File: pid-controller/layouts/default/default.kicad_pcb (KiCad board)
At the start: 2 copper layers, 210 x 60 mm, 26 parts, among them U17 1kΩ ±1% 100mW, U5 150Ω ±1% 100mW, U7 120Ω ±1% 100mW, U9 100Ω ±1% 100mW

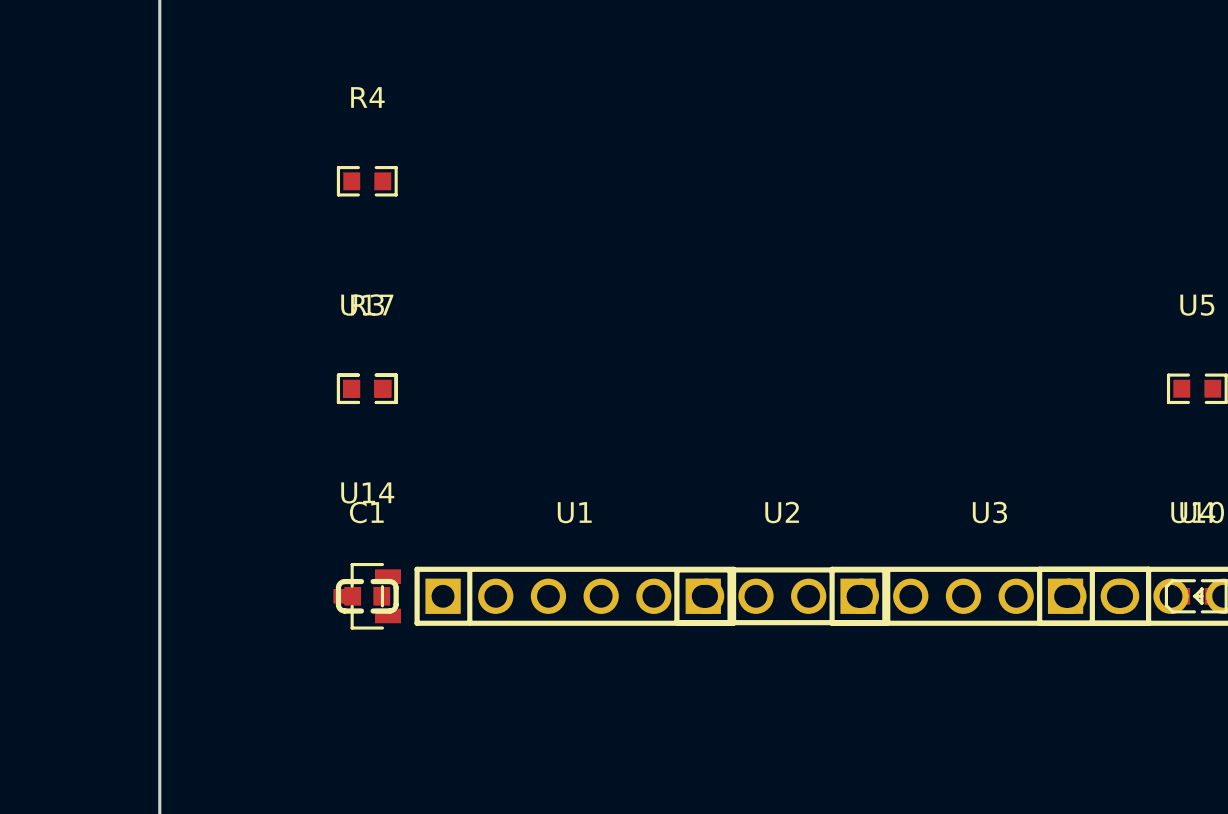
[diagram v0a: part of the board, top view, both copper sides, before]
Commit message: Add AC-DC converter and USB programming header
- Add HLK-PM01 AC-DC converter (100-240V AC → 5V DC @ 600mA)
- Add USB 4-pin header with Schottky diode for programming
- Add AC input connector for mains power
- Update main.ato to use on-board AC power instead of 5V input
- USB power OR-ing allows programming without AC connected

Co-Authored-By: Claude Opus 4.5 <noreply@anthropic.com>
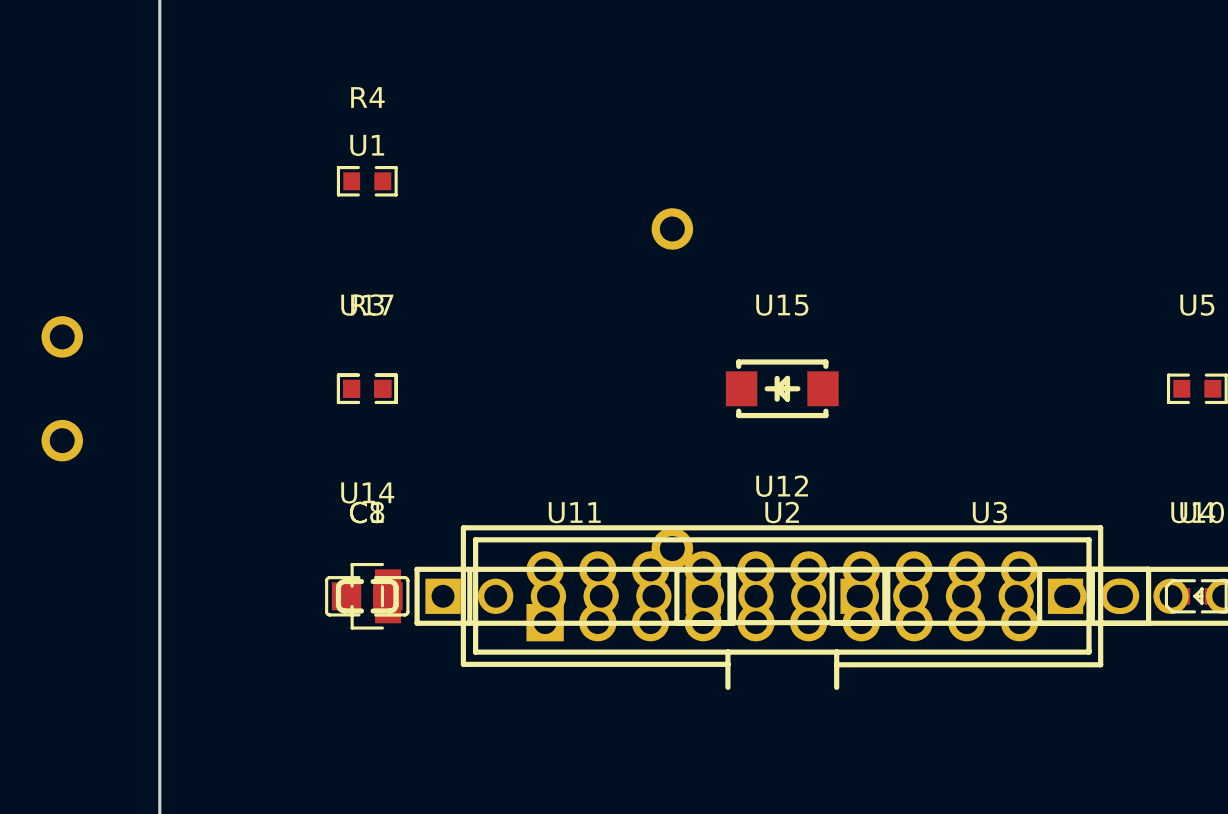
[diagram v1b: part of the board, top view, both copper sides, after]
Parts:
- added C8: 100µF ±20% 6.3V X5R, Murata_Electronics_GRM21BR60J107ME15L:C0805, F.Cu at (0.00, 0.00)
- added U11: , XFCN_PZ254V_11_06P:HDR-TH_6P-P2.54-V-M, F.Cu at (10.0, 0.00)
- added U12: , XFCN_BH254V_20P:CONN-TH_20P-P2.54_BH254V-20P, F.Cu at (20.0, 0.00)
- added U15: , MDD_Microdiode_Electronics_SS14:SMA_L4.2-W2.6-LS5.0-RD_1, F.Cu at (20.0, -10.0)
- U1: footprint XFCN_PZ254V_11_06P:HDR-TH_6P-P2.54-V-M -> HI_LINK_HLK_PM01:PWRM-TH_HLK-PM01
- moved U1 14.1 mm to (0.00, -10.0)
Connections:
- U1 pad 1: power_5v-VCC -> ac_line
- U1 pad 2: GND -> ac_neutral
- U1 pad 3: conn-net-0 -> GND
- U1 pad 4: conn-net-1 -> power_5v-VCC

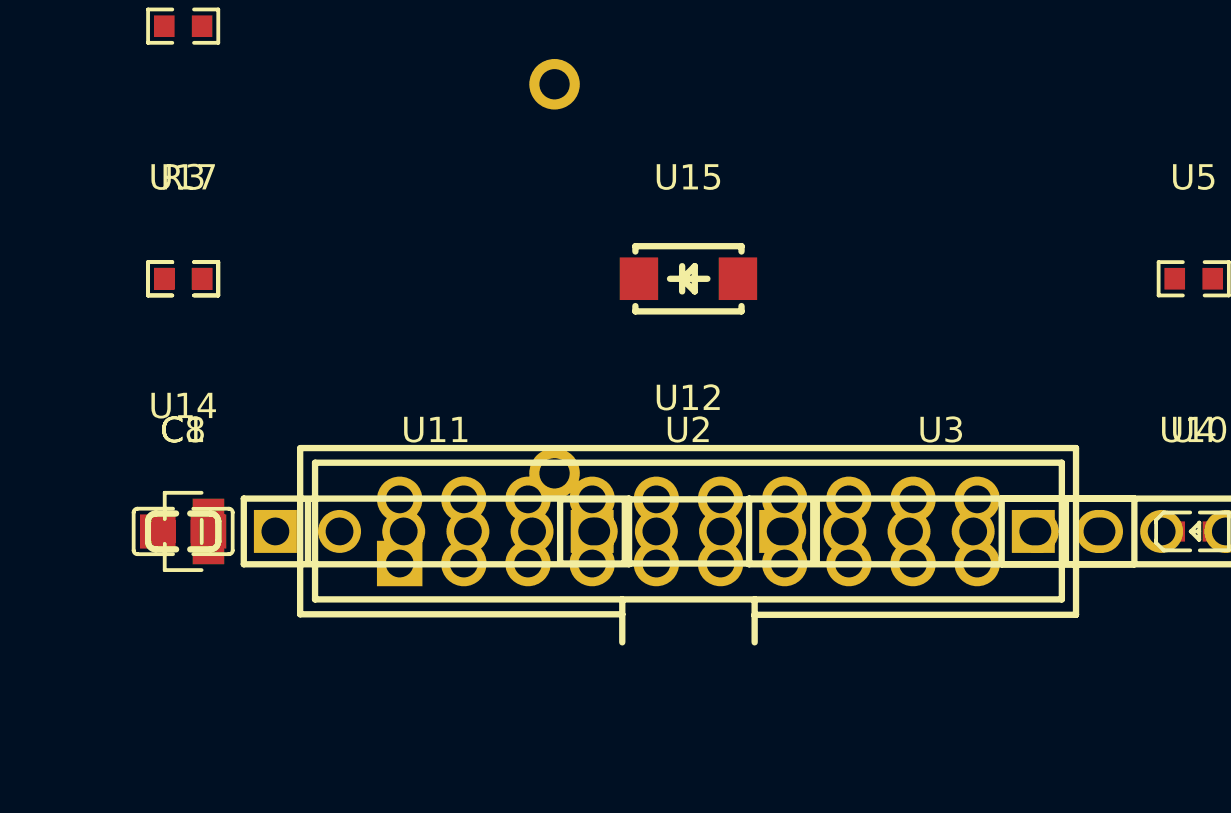
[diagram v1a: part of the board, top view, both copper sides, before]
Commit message: Switch to USB Type-C connector for programming
- Replace 4-pin USB header with USB Type-C (LCSC C393939)
- Add CC resistors (5.1k) for UFP device mode detection
- Pin mapping matches LCSC footprint exactly
- Schottky diode allows USB power when AC is off

Co-Authored-By: Claude Opus 4.5 <noreply@anthropic.com>
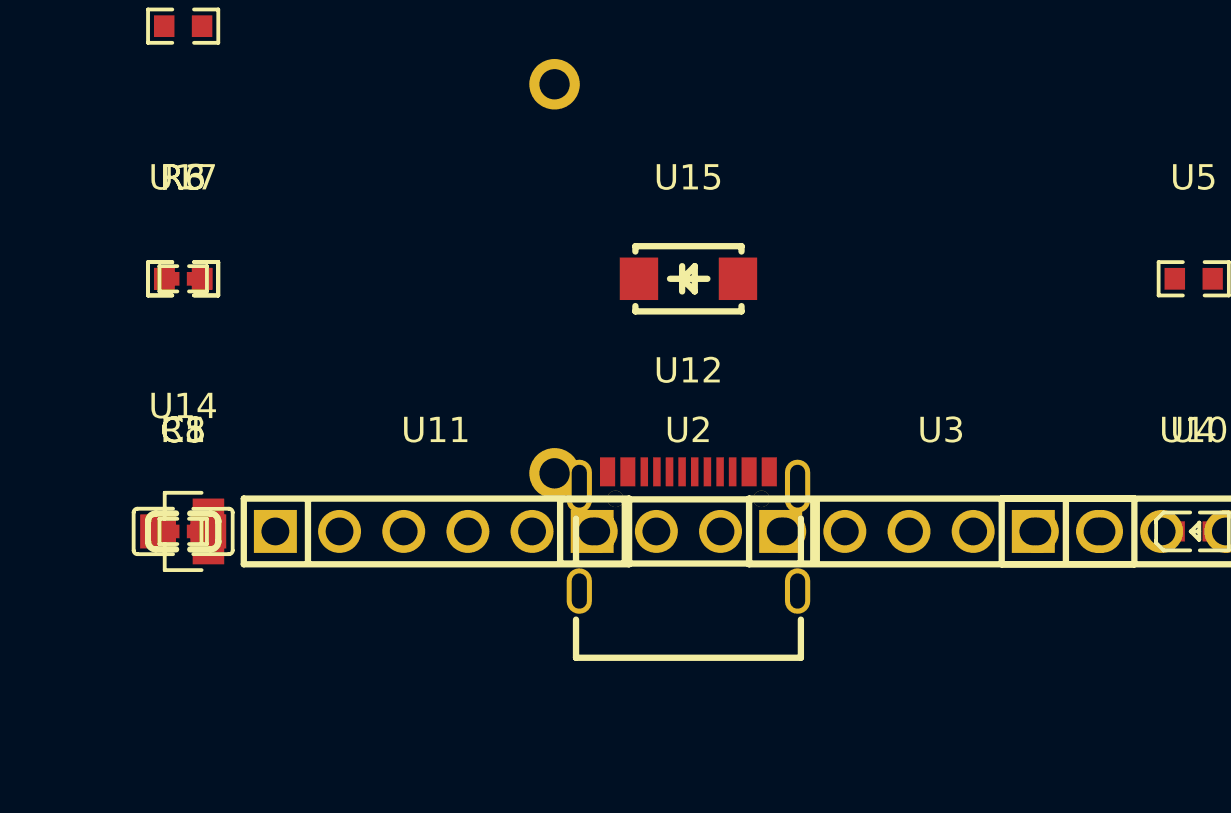
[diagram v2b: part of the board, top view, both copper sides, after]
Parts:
- added R5: 5.1kΩ ±1% 62.5mW, UNI_ROYAL_0402WGF5101TCE:R0402, F.Cu at (0.00, 0.00)
- added R6: 5.1kΩ ±1% 62.5mW, UNI_ROYAL_0402WGF5101TCE:R0402, F.Cu at (0.00, -10.0)
- U12: footprint XFCN_BH254V_20P:CONN-TH_20P-P2.54_BH254V-20P -> SHOU_HAN_TYPE_C16PIN:USB-C-SMD_TYPE-C16PIN
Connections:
- U12 pad 1: conn-anode -> GND
- U12 pad 2: usb_dm -> GND
- U12 pad 3: usb_dp -> GND
